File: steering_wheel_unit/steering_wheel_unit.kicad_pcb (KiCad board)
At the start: 2 copper layers, 90 x 70 mm, 129 parts, among them IC2 LM76202QPWPRQ1, J1 MAIN_CONNECTOR, J10 MODE2_SOCKET, J11 FUEL_CELL_SOCKET, J12 Additional goldpins, J14 LCD_SOCKET, J15 JTAG_SOCKET, J2 UJ20-C-V-C-3-SMT-TR, J3 HALF_GAS_SOCKET, J4 MODE1_SOCKET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

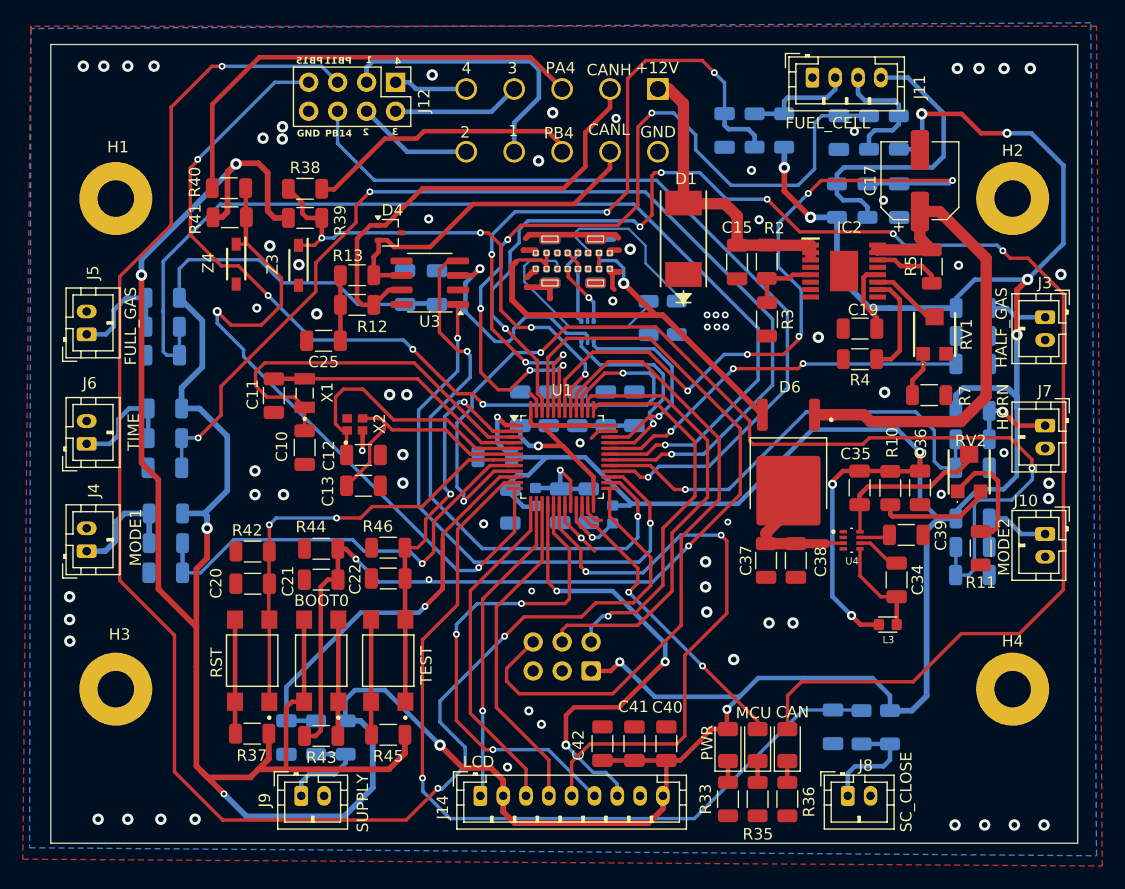
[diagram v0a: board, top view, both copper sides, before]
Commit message: Add no GND zones and logo
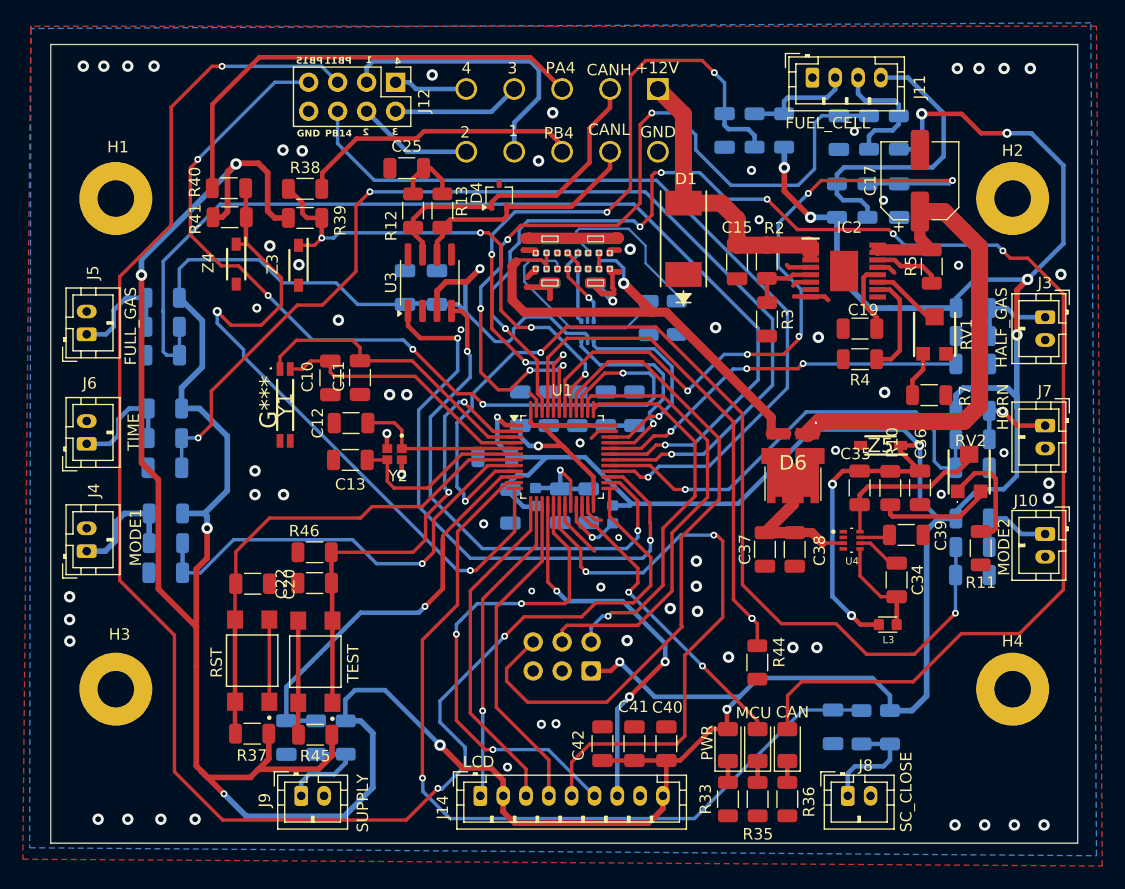
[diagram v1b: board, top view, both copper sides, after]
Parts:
- removed C21: 100n, Capacitor_SMD:C_1206_3216Metric
- removed R42, R43: 10k, Resistor_SMD:R_1206_3216Metric
- removed the SW2 at (165.6, 130.6)
- removed X1: 32k768, Lib:XTAL_NX3215SA-32.768K-STD-MUA-14
- added G***: LOGO, Lib:hydrogreen_grphics, B.Cu at (160.9, 107.9)
- added Y1: 9HT7-32.768KDZF-T, Lib:9HT732768KDZFT, F.Cu at (162.4, 108.2)
- added Z5: MMSZ3V3T1G, Lib:SOD3716X135N, F.Cu at (214.6, 111.7)
- C10, C11: value 5p1 -> 20p
- C12, C13: value 6p8 -> 12p
- D6: footprint Lib:DPAK228P990X239-4N -> Lib:V10K100DUHM3H
- Y2: renamed from X2; value 24M -> ABM11W-24.0000MHZ-8-D1X-T3; footprint Lib:OSC_NX2016SA-24MHZ-EXS00A-CS10820 -> Lib:XTAL_ABM11W-24.0000MHZ-8-D1X-T3
- moved R44 39.5 mm to (203.8, 130.8), turned to 90 degrees
- moved C25 16.8 mm to (173.0, 87.4)
- moved D4 10.1 mm to (181.2, 89.8), turned to 90 degrees
- moved R12 9.61 mm to (173.6, 91.2), turned to -90 degrees
- moved R13 9.38 mm to (176.2, 91.2), turned to -90 degrees
- moved C11 7.71 mm to (168.9, 105.8)
- moved C10 6.51 mm to (166.3, 105.8)
- moved C22 6.46 mm to (165.0, 123.8)
- moved R46 6.46 mm to (165.0, 121.1)
- moved R45 6.40 mm to (165.0, 137.1)
- moved SW2 6.39 mm to (165.0, 130.7)
- moved Y2 4.34 mm to (172.0, 112.5), turned to -90 degrees
- moved C12 3.00 mm to (168.2, 109.8), turned to 180 degrees
- moved C13 2.54 mm to (168.1, 113.0), turned to 180 degrees
- moved C37 0.98 mm to (204.4, 120.9)
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- renumbered SW3 to SW2
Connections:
- C10 pad 1: /MCU/LSE_IN -> /MCU/LSE_OUT
- C11 pad 1: /MCU/LSE_OUT -> /MCU/LSE_IN
- D6 pad 2: /POWER/VIN -> /POWER/Vreg
- R37 pad 2: Net-(SW1-A) -> /MCU/RESET
- R44 pad 1: /MCU/BOOT0 -> GND
- R44 pad 2: GND -> /MCU/BOOT0
- SW1 pad 1: /MCU/RESET -> GND
- SW1 pad 2: /MCU/RESET -> GND
- SW1 pad 3: Net-(SW1-A) -> /MCU/RESET
- SW1 pad 4: Net-(SW1-A) -> /MCU/RESET
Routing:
- net /MCU/BOOT0: track 89.6 -> 45.0 mm, vias 3 -> 2
- net GND: track 30.3 -> 51.6 mm, vias 73 -> 68
- net +3.3V: track 552.9 -> 539.6 mm
- net /CANH: track 40.3 -> 28.4 mm
- net Net-(R43-Pad1): track 10.3 -> 0.00 mm
- net Net-(SW1-A): track 10.0 -> 0.00 mm
- net /CANL: track 30.5 -> 21.3 mm
- net /MCU/HSE_IN: track 23.9 -> 15.3 mm
- net /MCU/LSE_IN: track 34.1 -> 26.4 mm
- net /LCD_CS: track 41.4 -> 34.5 mm
- net /MCU/TEST: track 35.3 -> 41.8 mm
- net /IO/CAN_TX: track 51.8 -> 45.9 mm
- net /MCU/HSE_OUT: track 21.6 -> 16.3 mm
- net /MCU/RESET: track 39.5 -> 43.9 mm, vias 2 -> 0
- net /VBUS: track 42.2 -> 45.4 mm
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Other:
- board text added: "Steering Wheel Unit Dawid Pisarczyk 28.03.2025"
- board text removed: "BOOT0"

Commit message: correct captions
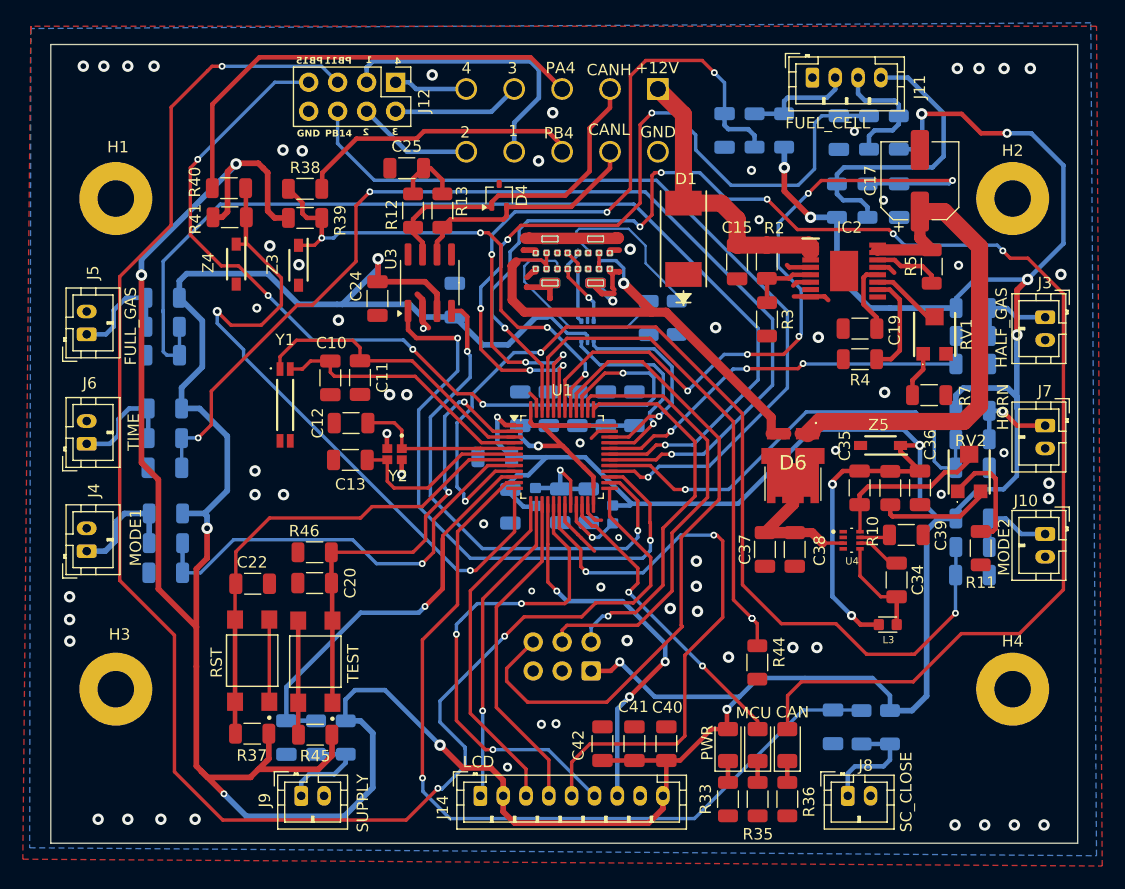
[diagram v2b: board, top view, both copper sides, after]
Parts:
- C24: moved to F.Cu
- moved C24 2.60 mm to (170.5, 98.9), turned to -90 degrees
- moved C23 1.91 mm to (177.3, 99.0)
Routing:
- net GND: track 51.6 -> 54.9 mm
- net /IO/FUEL_CELL_PREPARE_TO_RAC_BUTTON_MCU: track 74.1 -> 71.5 mm
- net +3.3V: track 539.6 -> 541.6 mm
- net /IO/FUEL_CELL_OFF_BUTTON_MCU: track 62.2 -> 63.1 mm
- net /IO/SPEED_RESET_BUTTON_MCU: track 95.8 -> 95.3 mm

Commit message: Add more gnd vias
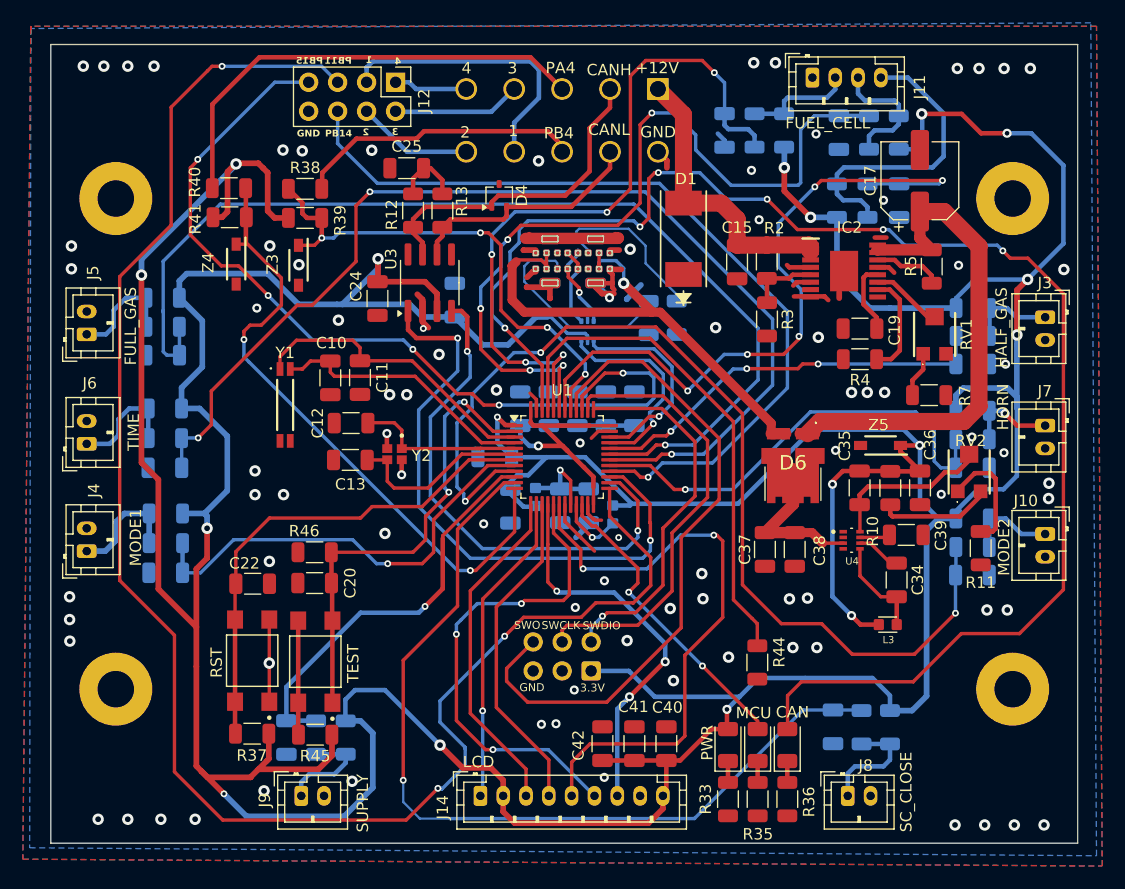
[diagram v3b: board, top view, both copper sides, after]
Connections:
- H1 pad 1: GND -> unconnected-(H1-Pad1)
- H2 pad 1: GND -> unconnected-(H2-Pad1)
- H3 pad 1: GND -> unconnected-(H3-Pad1)
- H4 pad 1: GND -> unconnected-(H4-Pad1)
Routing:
- net GND: track 54.9 -> 64.5 mm, vias 68 -> 87
- net /MCU/PA4: track 61.1 -> 55.4 mm
- net /IO/SC_CLOSE_BUTTON_MCU: track 74.2 -> 77.3 mm
- net /IO/FUEL_CELL_RACE_BUTTON_MCU: track 62.8 -> 61.1 mm
- net +3.3V: track 541.6 -> 541.0 mm, vias 19 -> 18
- net /MCU/USB_D-: track 6.46 -> 6.97 mm
- net /MCU/BOOT0: vias 2 -> 0
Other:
- board text added: "3.3V"
- board text added: "SWCLK"
- board text added: "SWDIO"
- board text added: "SWO"

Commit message: Add manufacturing
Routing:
- net GND: vias 87 -> 88
